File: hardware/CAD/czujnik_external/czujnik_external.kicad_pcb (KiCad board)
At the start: 2 copper layers, 50 x 30 mm, 4 parts, among them J1 8P8C, J2 PMS5003 socket, J3 DHT22 socket, J4 ADC socket

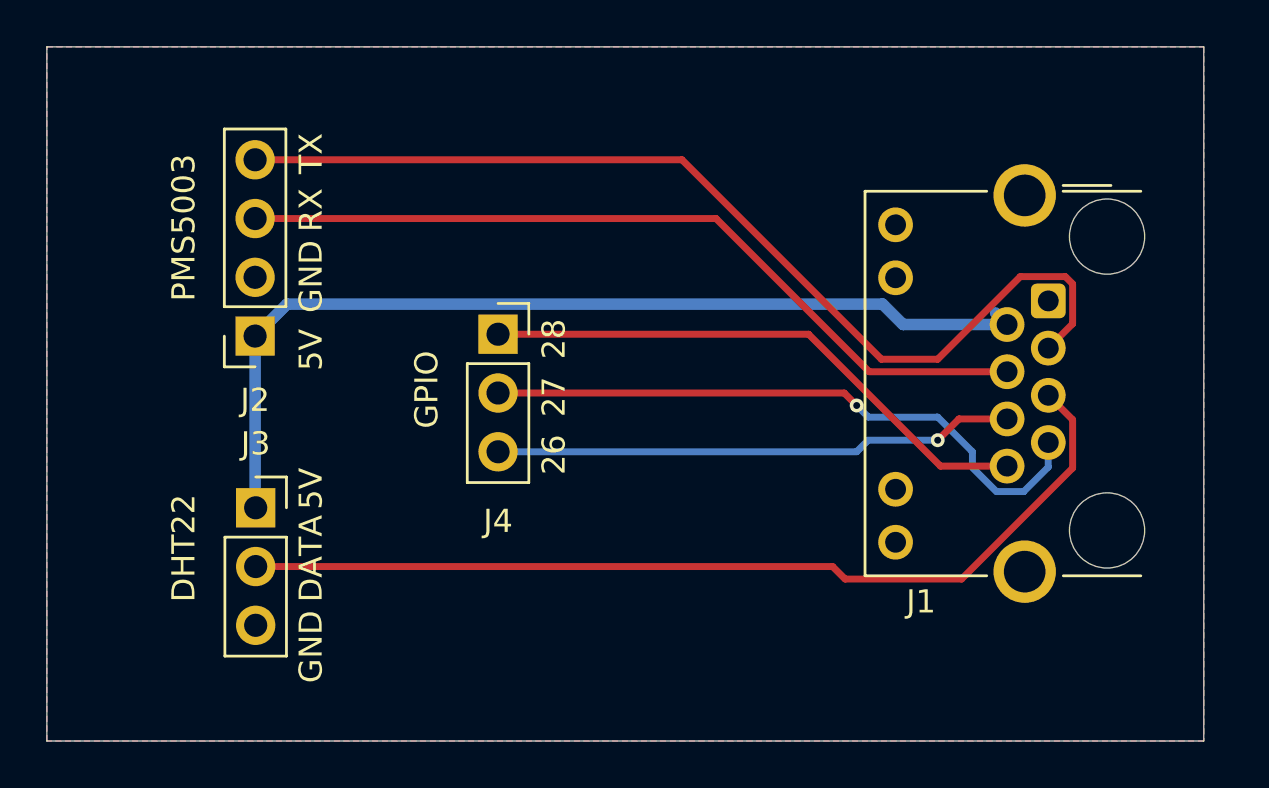
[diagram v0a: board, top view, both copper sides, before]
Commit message: refactor PCBs, add gerber files
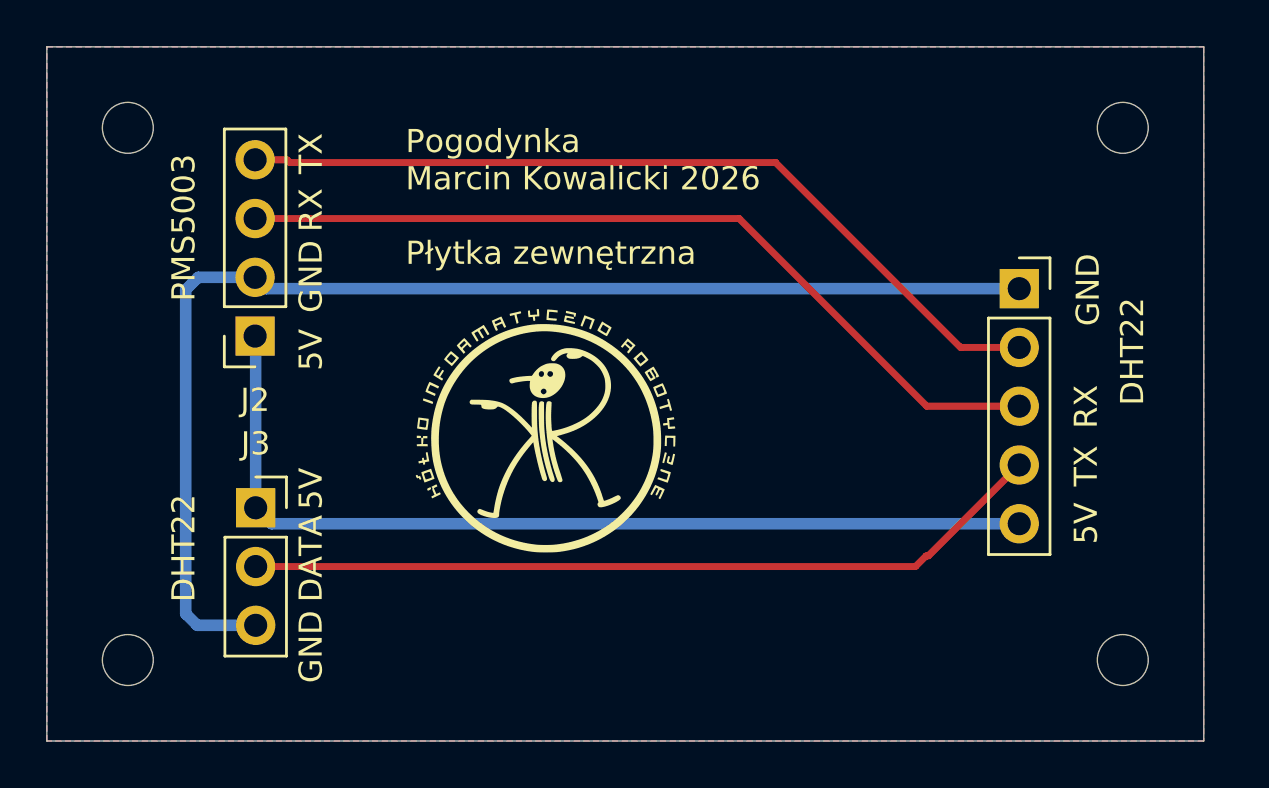
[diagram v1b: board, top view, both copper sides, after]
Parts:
- removed J1: 8P8C, Connector_RJ:RJ45_Connfly_DS1128-09-S8xx-S_Horizontal
- removed J4: ADC socket, Connector_PinSocket_2.54mm:PinSocket_1x03_P2.54mm_Vertical
- added GND: 5V, Connector_PinSocket_2.54mm:PinSocket_1x05_P2.54mm_Vertical, F.Cu at (172.5, 89.0)
- added REF**: MountingHole_2.2mm_M2, MountingHole:MountingHole_2.2mm_M2, F.Cu at (134.0, 105.0)
- added REF**: MountingHole_2.2mm_M2, MountingHole:MountingHole_2.2mm_M2, F.Cu at (177.0, 82.0)
- added REF**: MountingHole_2.2mm_M2, MountingHole:MountingHole_2.2mm_M2, F.Cu at (177.0, 105.0)
- added REF**: MountingHole_2.2mm_M2, MountingHole:MountingHole_2.2mm_M2, F.Cu at (134.0, 82.0)
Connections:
- J2 pad 3: /RX -> Net-(J2-Pin_3)
- J2 pad 4: /TX -> Net-(J2-Pin_4)
- J3 pad 2: Net-(J3-Pin_2) -> DHT22_D
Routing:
- net GND: track 0.00 -> 53.7 mm
- net /TX: track 43.7 -> 0.00 mm
- net Net-(J3-Pin_2): track 41.1 -> 0.00 mm
- net Net-(J2-Pin_4): track 0.00 -> 36.4 mm
- net Net-(J2-Pin_3): track 0.00 -> 36.4 mm
- net /RX: track 35.2 -> 0.00 mm
- net DHT22_D: track 0.00 -> 34.8 mm
- net Net-(J4-Pin_2): track 27.4 -> 0.00 mm, vias 1 -> 0
- net Net-(J4-Pin_1): track 24.4 -> 0.00 mm
- net Net-(J4-Pin_3): track 22.6 -> 0.00 mm, vias 1 -> 0
- net +5V: track 41.6 -> 40.7 mm
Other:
- board text added: "Pogodynka Marcin Kowalicki 2026 Płytka zewnętrzna"
- board text removed: "26"
- board text removed: "27"
- board text removed: "28"
- board text removed: "GPIO"

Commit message: add DB9 connectors to PCBs
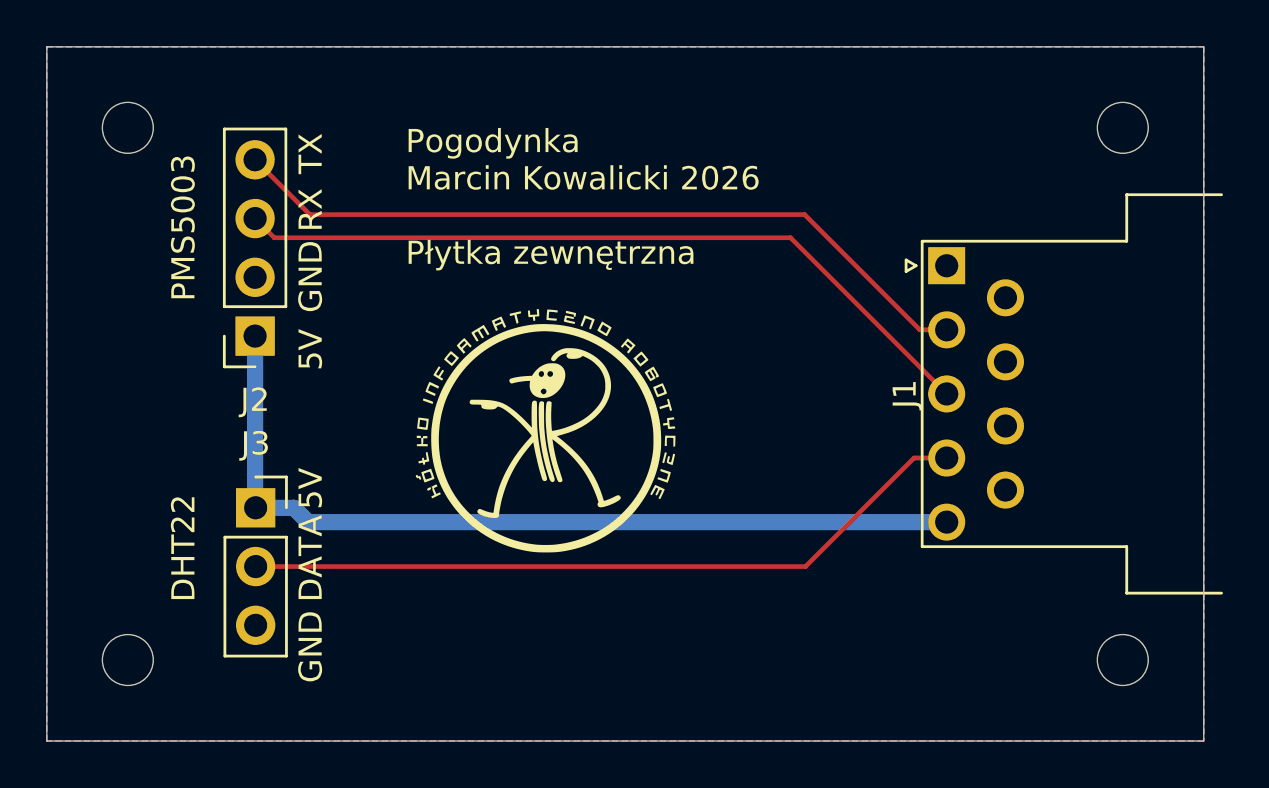
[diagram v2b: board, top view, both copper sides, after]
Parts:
- removed GND: 5V, Connector_PinSocket_2.54mm:PinSocket_1x05_P2.54mm_Vertical
- added J1: DE9_Socket, Connector_Dsub:DSUB-9_Socket_Horizontal_P2.77x2.54mm_EdgePinOffset9.40mm, F.Cu at (169.4, 88.0)
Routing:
- net GND: track 53.7 -> 0.00 mm
- net Net-(J2-Pin_4): track 36.4 -> 32.9 mm
- net Net-(J2-Pin_3): track 36.4 -> 33.0 mm
- net +5V: track 40.7 -> 37.6 mm
- net DHT22_D: track 34.8 -> 31.8 mm
